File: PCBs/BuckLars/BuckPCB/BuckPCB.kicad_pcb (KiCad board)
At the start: 2 copper layers, 100 x 100 mm, 57 parts, among them J1 Program_header, J2 Main board header, J3 12V, J4 5V, J5 POWER_IN, Q1 IRLIZ44N, Q2 IRLIZ44N, Q3 IRLIZ44N, Q4 IRLIZ44N, SW1 RESET, SW2 BOOT, U1 ESP32-WROOM-32D, U2 LT1936, U3 LF2304NTR, U4 LF2304NTR

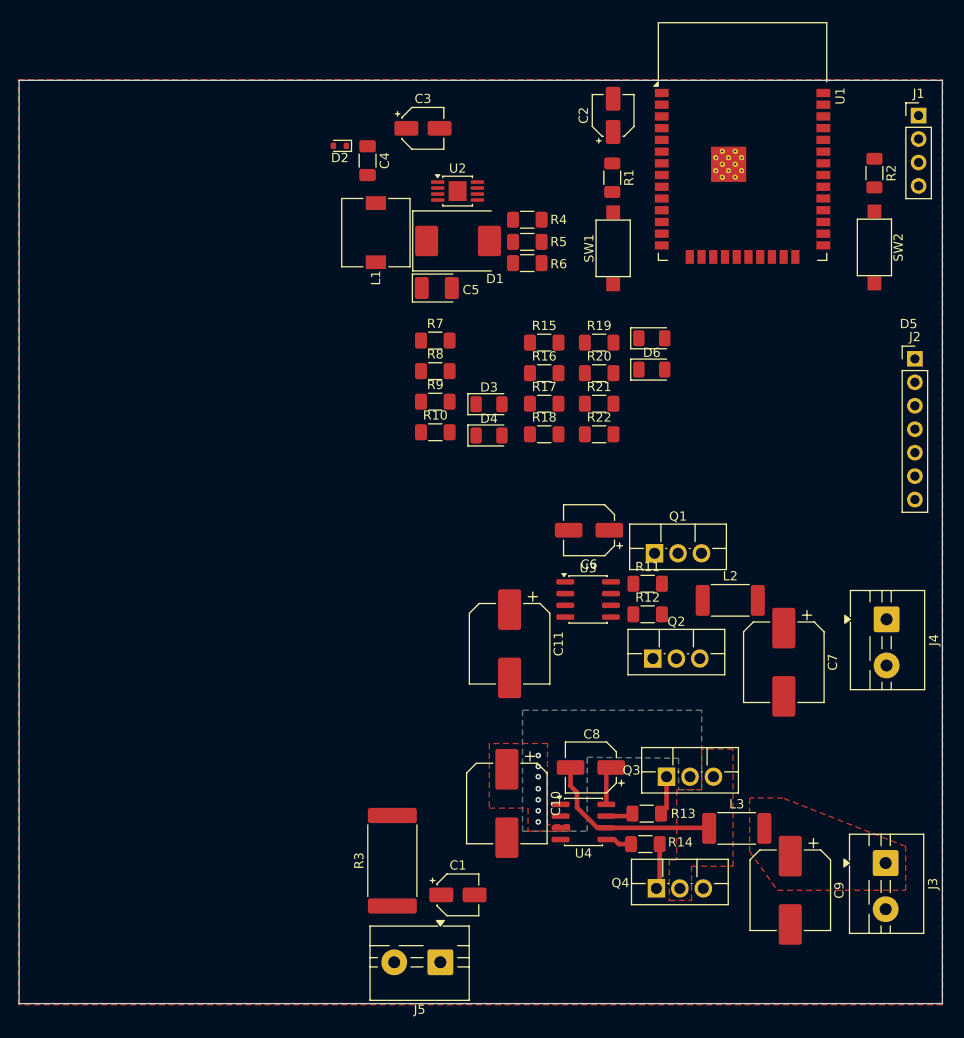
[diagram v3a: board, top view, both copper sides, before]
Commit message: changed footprints buck
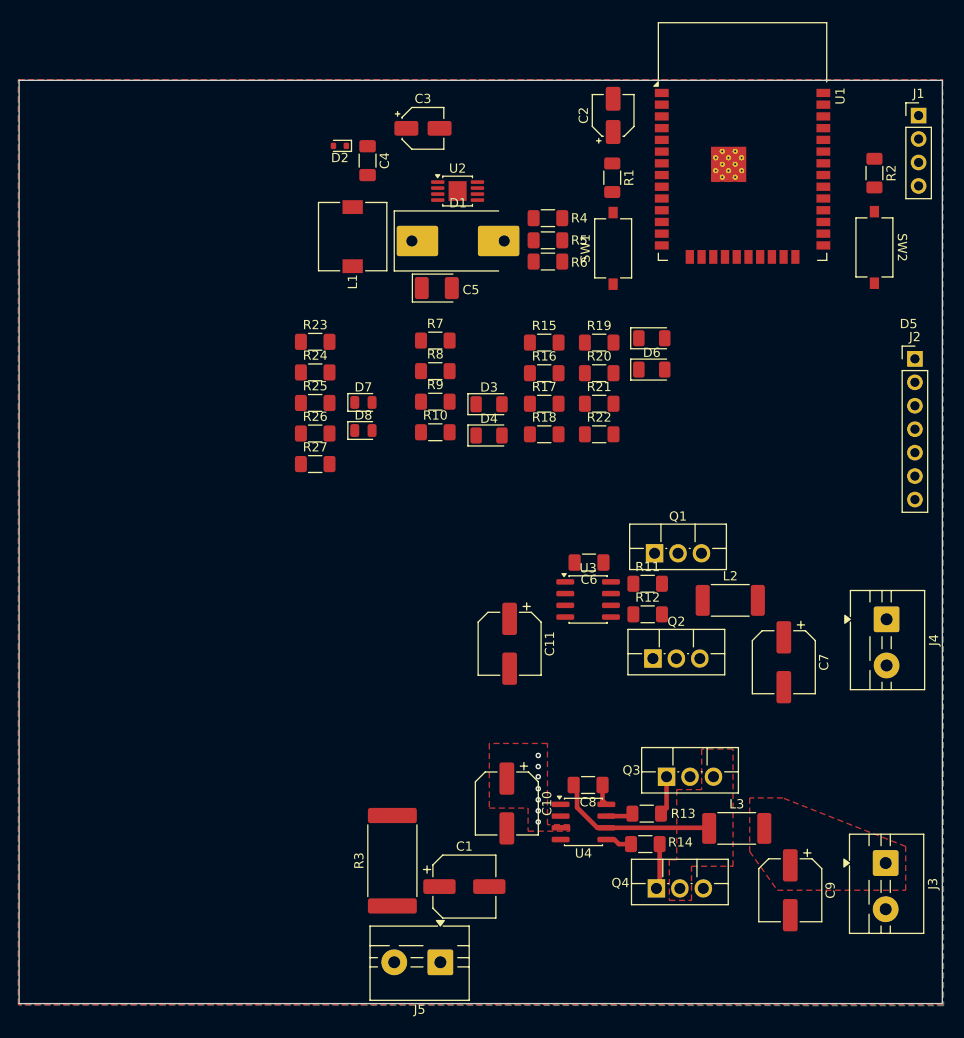
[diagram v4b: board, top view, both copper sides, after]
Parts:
- added D7: LED, LED_SMD:LED_0805_2012Metric, F.Cu at (133.9, 96.7)
- added D8: LED, LED_SMD:LED_0805_2012Metric, F.Cu at (133.9, 99.7)
- added R23: 10K, Resistor_SMD:R_1206_3216Metric_Pad1.30x1.75mm_HandSolder, F.Cu at (128.6, 90.1)
- added R24: 4k7, Resistor_SMD:R_1206_3216Metric_Pad1.30x1.75mm_HandSolder, F.Cu at (128.6, 93.4)
- added R25: 4k7, Resistor_SMD:R_1206_3216Metric_Pad1.30x1.75mm_HandSolder, F.Cu at (128.6, 96.7)
- added R26: 1k, Resistor_SMD:R_1206_3216Metric_Pad1.30x1.75mm_HandSolder, F.Cu at (128.6, 100.0)
- added R27: 1k, Resistor_SMD:R_1206_3216Metric_Pad1.30x1.75mm_HandSolder, F.Cu at (128.6, 103.3)
- C1: value 47U -> 47u 35V; footprint Capacitor_SMD:CP_Elec_4x5.3 -> Capacitor_SMD:CP_Elec_6.3x5.7
- C10, C11, C7, C9: value 100u -> 47u 35V; footprint Capacitor_SMD:CP_Elec_8x10.5 -> Capacitor_SMD:CP_Elec_6.3x5.7
- C2: value 10U -> 4,7u
- C6, C8: value C_Polarized -> 100n; footprint Capacitor_SMD:CP_Elec_5x5.4 -> Capacitor_SMD:C_1206_3216Metric_Pad1.33x1.80mm_HandSolder
- D1: footprint Diode_SMD:D_SMC -> Diode_SMD:D_SMC-RM10_Universal_Handsoldering
- L1: value 10uH -> 10u
- SW1, SW2: footprint Button_Switch_SMD:SW_SPST_CK_RS282G05A3 -> Button_Switch_SMD:SW_Tactile_SPST_NO_Straight_CK_PTS636Sx25SMTRLFS
- moved C6 3.50 mm to (158.3, 114.0)
- moved L1 2.55 mm to (132.7, 78.7)
- moved R4 2.24 mm to (153.8, 76.7)
- moved R5 2.24 mm to (153.8, 79.1)
- moved R6 2.24 mm to (153.8, 81.4)
- moved C8 1.92 mm to (158.2, 138.1)
- moved C1 1.14 mm to (144.8, 149.1)
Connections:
- J2 pad 1: +BATT -> Imeasure
- J2 pad 2: +BATT -> Imeasure
- U1 pad 26: unconnected-(U1-IO4-Pad26) -> Net-(U1-IO4)
- U1 pad 29: unconnected-(U1-IO5-Pad29) -> Net-(U1-IO5)
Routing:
- net Net-(Q3-S): track 19.9 -> 16.9 mm
- net Net-(U4-VB): track 4.21 -> 2.27 mm

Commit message: wired second buck converter
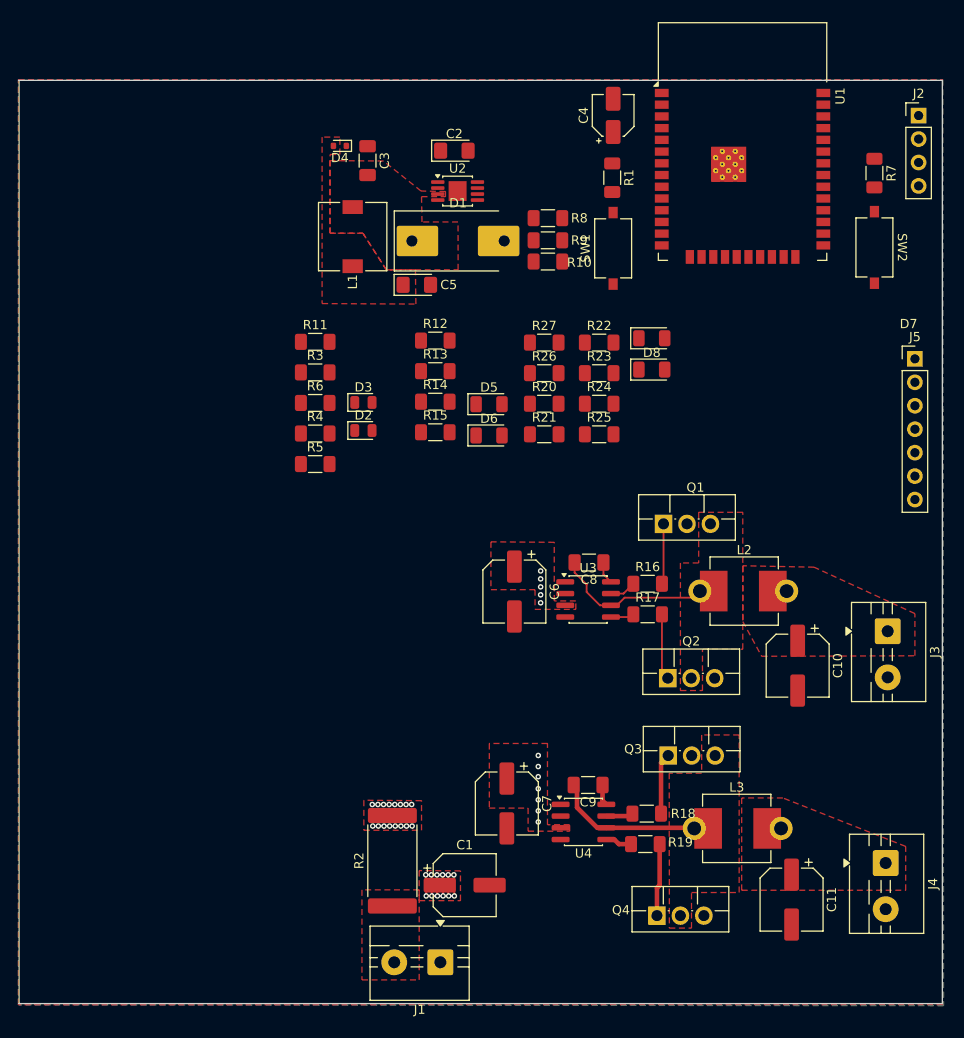
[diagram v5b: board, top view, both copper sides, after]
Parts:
- removed the C3 at (140.3, 67.0)
- added C2: 4.7u 50V, Diode_SMD:D_1206_3216Metric_Pad1.42x1.75mm_HandSolder, F.Cu at (143.7, 69.4)
- C5: value 22uF 16V -> 47u 6.3V; footprint Capacitor_Tantalum_SMD:CP_EIA-3528-12_Kemet-T_HandSolder -> Diode_SMD:D_1206_3216Metric_Pad1.42x1.75mm_HandSolder
- L2, L3: footprint Inductor_SMD:L_2512_6332Metric_Pad1.52x3.35mm_HandSolder -> Inductor_SMD:L_7.3x7.3_H4.5
- moved C6 5.68 mm to (150.2, 117.1)
- moved Q1 3.33 mm to (166.4, 109.8)
- moved Q4 2.95 mm to (165.7, 152.2)
- moved Q2 2.67 mm to (166.8, 126.5)
- moved Q3 2.30 mm to (166.9, 134.9)
- moved C5 2.19 mm to (139.6, 83.9)
- moved L2 1.81 mm to (175.1, 117.1)
- moved C10 1.54 mm to (180.9, 125.2)
- moved J3 1.30 mm to (190.7, 121.4)
- moved C11 1.02 mm to (180.2, 150.5)
- moved C1 0.16 mm to (144.8, 148.9)
- renumbered C7 to C10, C9 to C11, C4 to C3, C2 to C4, C11 to C6, C10 to C7, C6 to C8, C8 to C9, D8 to D2, D7 to D3, D2 to D4, D3 to D5, D4 to D6, D5 to D7, D6 to D8, J5 to J1, J1 to J2, J4 to J3, J3 to J4, J2 to J5, R6 to R10, R23 to R11, R7 to R12, R8 to R13, R9 to R14, R10 to R15, R11 to R16, R12 to R17, R13 to R18, R14 to R19, R3 to R2, R17 to R20, R18 to R21, R19 to R22, R20 to R23, R21 to R24, R22 to R25, R16 to R26, R15 to R27, R24 to R3, R26 to R4, R27 to R5, R25 to R6, R2 to R7, R4 to R8, R5 to R9
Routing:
- net Imeasure: track 0.00 -> 19.9 mm, vias 0 -> 40
- net Net-(Q1-S): track 0.00 -> 17.2 mm
- net Net-(Q2-G): track 0.00 -> 7.18 mm
- net Net-(Q1-G): track 0.00 -> 6.56 mm
- net Net-(Q4-G): track 4.94 -> 7.87 mm
- net Net-(U3-HO): track 0.00 -> 2.87 mm
- net Net-(U3-LO): track 0.00 -> 2.55 mm
- net Net-(U3-VB): track 0.00 -> 2.43 mm
- net Net-(Q3-G): track 4.25 -> 6.61 mm
- net +BATT: vias 7 -> 0
- added copper zone on F.Cu, net +3.3V
- added copper zone on B.Cu, net Imeasure
- added copper zone on F.Cu, net Imeasure
- added copper zone on F.Cu, net Net-(C10-Pad1)
- added copper zone on F.Cu, net Net-(D1-K)
- added copper zone on F.Cu, net Net-(Q1-S)
- removed copper zone on B.Cu, net +BATT
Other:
- board text added: "POWER_IN"

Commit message: added 5V buck
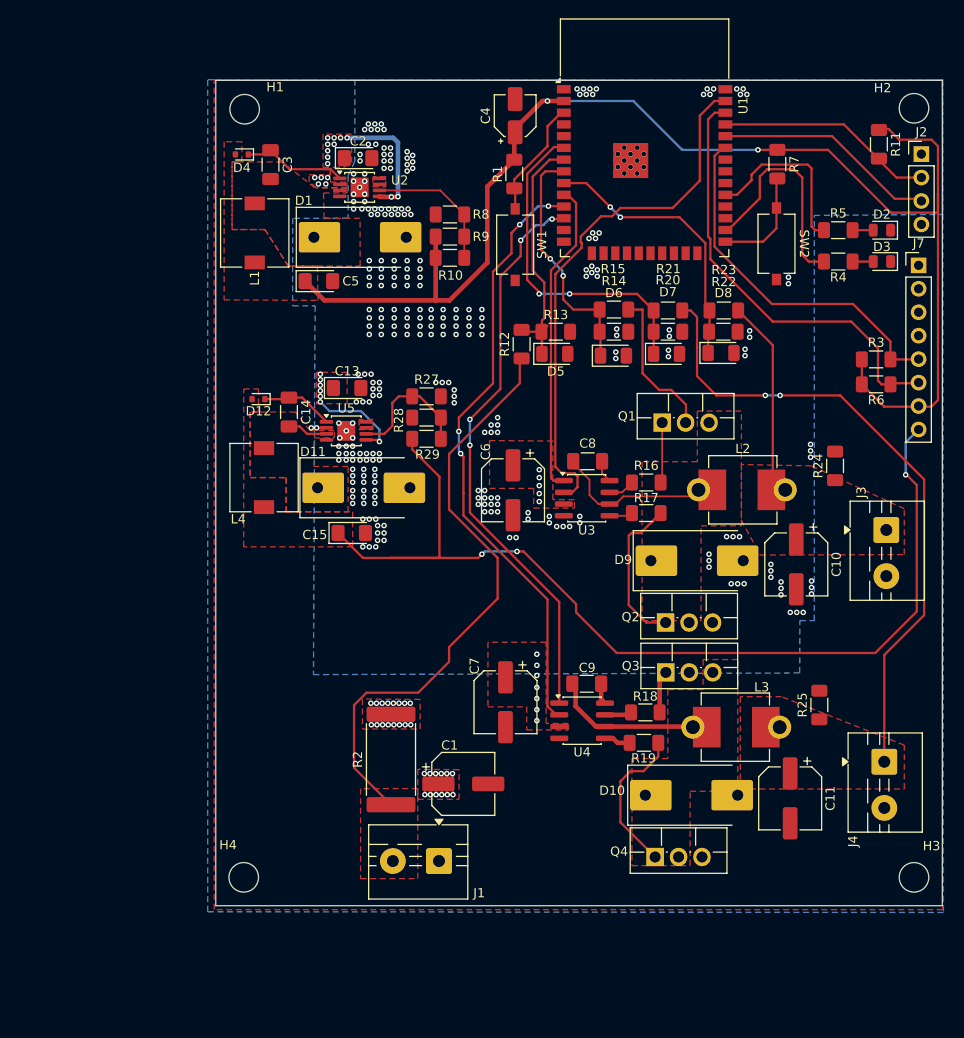
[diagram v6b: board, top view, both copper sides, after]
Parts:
- removed J5: Main board header, Connector_PinHeader_2.54mm:PinHeader_1x07_P2.54mm_Vertical
- removed R26: 0.1, Resistor_SMD:R_1206_3216Metric_Pad1.30x1.75mm_HandSolder
- added C13: 4.7u 50V, Diode_SMD:D_1206_3216Metric_Pad1.42x1.75mm_HandSolder, F.Cu at (132.1, 95.1)
- added C14: 0.22uF, Capacitor_SMD:C_1206_3216Metric_Pad1.33x1.80mm_HandSolder, F.Cu at (125.8, 97.7)
- added C15: 47u 6.3V, Diode_SMD:D_1206_3216Metric_Pad1.42x1.75mm_HandSolder, F.Cu at (132.6, 110.8)
- added D10: SK36A, Diode_SMD:D_SMC-RM10_Universal_Handsoldering, F.Cu at (169.4, 139.2)
- added D11: SK36A, Diode_SMD:D_SMC-RM10_Universal_Handsoldering, F.Cu at (133.9, 105.9)
- added D12: 1N4148WT, Diode_SMD:D_SOD-523, F.Cu at (122.5, 96.3)
- added D9: SK36A, Diode_SMD:D_SMC-RM10_Universal_Handsoldering, F.Cu at (170.0, 113.8)
- added H1: MountingHole, MountingHole:MountingHole_3.2mm_M3_ISO14580, F.Cu at (121.0, 64.9)
- added H2: MountingHole, MountingHole:MountingHole_3.2mm_M3_ISO14580, F.Cu at (193.5, 64.8)
- added H3: MountingHole, MountingHole:MountingHole_3.2mm_M3_ISO14580, F.Cu at (193.5, 148.1)
- added H4: MountingHole, MountingHole:MountingHole_3.2mm_M3_ISO14580, F.Cu at (120.9, 148.1)
- added J7: Conn_01x08_Pin, Connector_PinHeader_2.54mm:PinHeader_1x08_P2.54mm_Vertical, F.Cu at (194.0, 81.8)
- added L4: 10u, Inductor_SMD:L_7.3x7.3_H4.5, F.Cu at (123.1, 104.8)
- added R28: 1.8K, Resistor_SMD:R_1206_3216Metric_Pad1.30x1.75mm_HandSolder, F.Cu at (140.7, 98.3)
- added R29: 5.7k, Resistor_SMD:R_1206_3216Metric_Pad1.30x1.75mm_HandSolder, F.Cu at (140.7, 100.6)
- added U5: LT1936, Package_SO:MSOP-8-1EP_3x3mm_P0.65mm_EP1.95x2.15mm, F.Cu at (132.0, 99.7)
- R27: value 0.1 -> 1.8K
- moved R11 64.7 mm to (189.7, 68.7), turned to -90 degrees
- moved R5 62.1 mm to (185.3, 78.0)
- moved R6 60.8 mm to (189.4, 94.7)
- moved R3 60.8 mm to (189.4, 92.0)
- moved D2 60.2 mm to (190.0, 78.0), turned to 180 degrees
- moved R4 59.6 mm to (185.3, 81.4)
- moved D3 58.2 mm to (190.0, 81.4), turned to 180 degrees
- moved R25 37.8 mm to (183.2, 129.4), turned to 90 degrees
- moved R24 26.4 mm to (184.9, 103.5), turned to 90 degrees
- moved R15 22.2 mm to (161.0, 89.0)
- moved R14 21.8 mm to (161.0, 86.6), turned to 180 degrees
- moved R21 17.4 mm to (166.8, 89.0)
- moved R20 16.8 mm to (166.8, 86.7), turned to 180 degrees
- moved D6 16.0 mm to (160.9, 91.6)
- moved R23 14.2 mm to (172.8, 89.0)
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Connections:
- C10 pad 1: Net-(C10-Pad1) -> Vbuck
- C11 pad 1: Net-(C11-Pad1) -> +12V
- J3 pad 1: +5V -> Vbuck
- L2 pad 2: Net-(C10-Pad1) -> Vbuck
- L3 pad 2: Net-(C11-Pad1) -> +12V
- R22 pad 1: +5V -> Vbuck
- R24 pad 1: Net-(C10-Pad1) -> Vbuck
- R25 pad 1: Net-(C11-Pad1) -> +12V
- R27 pad 1: Net-(C11-Pad1) -> Net-(U5-FB)
- R27 pad 2: +12V -> GND
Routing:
- net +3.3V: track 0.00 -> 149.3 mm, vias 0 -> 2
- net +5V: track 0.00 -> 111.3 mm, vias 0 -> 3
- net +12V: track 0.00 -> 69.9 mm, vias 0 -> 2
- net HI2: track 0.00 -> 66.1 mm, vias 0 -> 4
- net +BATT: track 0.00 -> 65.1 mm
- net LO2: track 0.00 -> 62.1 mm, vias 0 -> 4
- net HI1: track 0.00 -> 58.1 mm
- net SCL: track 0.00 -> 47.7 mm
- net Imeasure: track 19.9 -> 62.2 mm, vias 40 -> 65
- net SDA: track 0.00 -> 39.7 mm
- net V12: track 0.00 -> 36.8 mm, vias 0 -> 2
- net LO1: track 0.00 -> 34.1 mm
- net V5: track 0.00 -> 30.7 mm, vias 0 -> 2
- net Vb: track 0.00 -> 29.5 mm
- net Vm: track 0.00 -> 26.5 mm, vias 0 -> 2
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- added copper zone on F.Cu, net +12V
- added copper zone on F.Cu, net +5V
- added copper zone on B.Cu, net GND
- added copper zone on F.Cu, net Net-(D11-K)
- added copper zone on F.Cu, net Net-(U2-COMP)
- added copper zone on F.Cu, net Net-(U5-COMP)
- added copper zone on F.Cu, net Vbuck
- removed copper zone on F.Cu, net Net-(C10-Pad1)
- removed copper zone on F.Cu, net Net-(C11-Pad1)
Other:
- board size 100 x 100 mm -> 78.7 x 89.4 mm

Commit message: added qr code and status leds
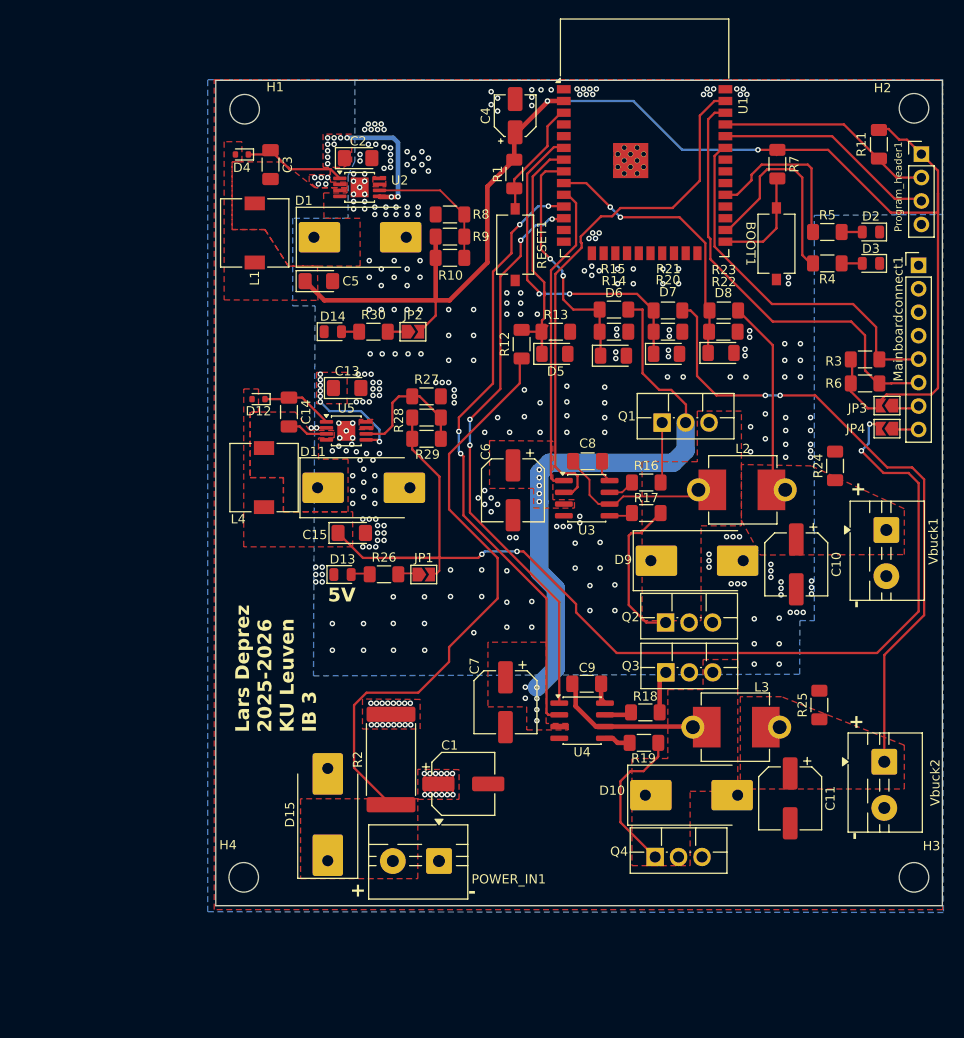
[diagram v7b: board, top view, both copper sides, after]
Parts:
- added D13: LED, LED_SMD:LED_0805_2012Metric, F.Cu at (131.6, 115.3)
- added D14: LED, LED_SMD:LED_0805_2012Metric, F.Cu at (130.6, 89.0)
- added D15: SK36A, Diode_SMD:D_SMC-RM10_Universal_Handsoldering, F.Cu at (130.0, 141.3)
- added JP1: SolderJumper_2_Open, Jumper:SolderJumper-2_P1.3mm_Open_TrianglePad1.0x1.5mm, F.Cu at (140.4, 115.3)
- added JP2: SolderJumper_2_Open, Jumper:SolderJumper-2_P1.3mm_Open_TrianglePad1.0x1.5mm, F.Cu at (139.2, 89.0)
- added JP3: SolderJumper_2_Open, Jumper:SolderJumper-2_P1.3mm_Open_TrianglePad1.0x1.5mm, F.Cu at (190.6, 97.0)
- added JP4: SolderJumper_2_Open, Jumper:SolderJumper-2_P1.3mm_Open_TrianglePad1.0x1.5mm, F.Cu at (190.6, 99.5)
- added R26: 2.2k, Resistor_SMD:R_1206_3216Metric_Pad1.30x1.75mm_HandSolder, F.Cu at (136.1, 115.3)
- added R30: 1K, Resistor_SMD:R_1206_3216Metric_Pad1.30x1.75mm_HandSolder, F.Cu at (134.9, 89.0)
- Vbuck1: renamed from J3; value 5V -> Vbuck
- moved D2 1.20 mm to (188.8, 78.2)
- moved R5 1.20 mm to (184.1, 78.2)
- moved D3 1.20 mm to (188.8, 81.6)
- moved R4 1.20 mm to (184.1, 81.6)
- moved R6 1.20 mm to (188.2, 94.6)
- moved R3 1.20 mm to (188.2, 92.0)
- renumbered SW2 to BOOT1, J7 to Mainboardconnect1, J1 to POWER_IN1, J2 to Program_header1, SW1 to RESET1, J4 to Vbuck2
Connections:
- net Net-(J2-Pin_2) renamed /TX
- net Net-(J2-Pin_3) renamed /RX
- Mainboardconnect1 pad 7: +3.3V -> Net-(JP3-A)
- Mainboardconnect1 pad 8: +5V -> Net-(JP4-A)
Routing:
- net Imeasure: track 62.2 -> 106.9 mm, vias 65 -> 64
- net +5V: track 111.3 -> 121.6 mm, vias 3 -> 4
- net +3.3V: track 149.3 -> 153.5 mm
- net Net-(JP4-A): track 0.00 -> 2.90 mm
- net Net-(JP3-A): track 0.00 -> 2.88 mm
- net Net-(JP1-A): track 0.00 -> 2.04 mm
- net Net-(D13-A): track 0.00 -> 2.02 mm
- net Net-(JP2-A): track 0.00 -> 2.00 mm
- net Net-(D14-A): track 0.00 -> 1.91 mm
- net Net-(U1-IO4): track 23.8 -> 22.7 mm
- net SDA: track 39.7 -> 40.7 mm
- net Net-(U1-IO5): track 19.0 -> 18.2 mm
- net GND: vias 274 -> 298
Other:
- board text added: "+"
- board text added: "-"
- board text added: "3V3 TX-> RX<- GND"
- board text added: "5V"
- board text added: "Lars Deprez 2025-2026 KU Leuven IB 3"
- board text added: "VBatt Vbatt GND GND SDA SCL 3V3 5V"
- board text removed: "POWER_IN"

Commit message: generated gerbers
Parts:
- added JP5: SolderJumper_2_Open, Jumper:SolderJumper-2_P1.3mm_Open_TrianglePad1.0x1.5mm, B.Cu at (125.0, 149.6)
- added JP6: SolderJumper_2_Open, Jumper:SolderJumper-2_P1.3mm_Open_TrianglePad1.0x1.5mm, B.Cu at (125.0, 143.8)
- added POWER_IN2: POWER_IN, TerminalBlock:TerminalBlock_MaiXu_MX126-5.0-02P_1x02_P5.00mm, F.Cu at (153.7, 146.4)
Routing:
- net +BATT: vias 0 -> 22
- added copper zone on B.Cu, net +BATT
